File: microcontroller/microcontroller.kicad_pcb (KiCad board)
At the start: 2 copper layers, 70 x 39 mm, 46 parts, among them J1 Conn_01x05_Pin, J2 Conn_01x10_Pin, J3 USB_C_Receptacle, J4 Conn_01x04_Pin, SW1 SW_SPST, SW2 SW_SPST, SW3 SW_SPST, U1 DS3231MZ, U2 AMS1117-3.3, U3 STM32F103CBTx, Y1 8Mhz

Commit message: Changed connectors
Changed connector from mcu to power supply to idc.
All switches now use a straight pinheader, with no pullups (now using
mcu pulldowns).
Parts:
- removed the R1 at (137.3, 96.3)
- removed the R2 at (141.1, 96.3)
- removed the R3 at (144.8, 96.3)
- removed SW1, SW2, SW3: SW_SPST, Connector_PinHeader_2.54mm:PinHeader_1x02_P2.54mm_Vertical
- added J2: Conn_01x04_Pin, Connector_PinHeader_2.54mm:PinHeader_1x04_P2.54mm_Vertical, F.Cu at (142.1, 91.9)
- J1: value Conn_01x05_Pin -> Conn_01x04_Pin; footprint Connector_PinHeader_2.54mm:PinHeader_1x05_P2.54mm_Vertical -> Connector_PinHeader_2.54mm:PinHeader_1x04_P2.54mm_Vertical
- J3: renamed from J2; footprint Connector_PinHeader_2.54mm:PinHeader_1x10_P2.54mm_Vertical -> Connector_IDC:IDC-Header_2x05_P2.54mm_Vertical
- moved R3 23.3 mm to (119.9, 82.2), turned to 90 degrees
- moved D1 18.7 mm to (119.9, 85.3), turned to -90 degrees
- moved J3 17.0 mm to (178.4, 80.4), turned to 0 degrees
- moved JP1 9.43 mm to (119.9, 91.3), turned to 180 degrees
- moved R9 9.31 mm to (127.9, 99.9), turned to 180 degrees
- moved R8 5.26 mm to (130.9, 99.9), turned to 0 degrees
- moved J1 4.18 mm to (142.1, 99.9)
- moved U1 0.59 mm to (128.5, 92.1)
- moved C1 0.58 mm to (124.1, 90.6)
- renumbered J3 to J4, J4 to J5, R4 to R1, R5 to R2, R6 to R3, R7 to R4, R8 to R5, R9 to R6, R10 to R7, R11 to R8, R12 to R9
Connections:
- J1 pad 1: GND -> ADJUST_SW
- J1 pad 2: SECOND_SW_H -> MODE_SW
- J1 pad 3: MINUTE_SW_H -> POWER_SW
- J1 pad 4: HOUR_SW_H -> +3V3
- U3 pad 13: ADJUST_SW -> SECOND_SW_H
- U3 pad 14: MODE_SW -> MINUTE_SW_H
- U3 pad 15: POWER_SW -> HOUR_SW_H
- U3 pad 16: HOUR_SW_H -> POWER_SW
- U3 pad 17: MINUTE_SW_H -> MODE_SW
- U3 pad 18: SECOND_SW_H -> ADJUST_SW
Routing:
- net +3V3: track 162.1 -> 202.8 mm, vias 2 -> 0
- net VBUS: track 37.7 -> 59.8 mm
- net LATCH: track 11.3 -> 21.4 mm, vias 0 -> 2
- net OE: track 12.5 -> 17.5 mm, vias 0 -> 2
- net ADJUST_SW: track 20.3 -> 25.1 mm
- net CLK: track 12.0 -> 16.2 mm, vias 0 -> 2
- net MODE_SW: track 25.0 -> 27.7 mm
- net SECOND_SW_H: track 24.5 -> 22.2 mm
- net GND: track 41.8 -> 40.5 mm, vias 29 -> 26
- net SER: track 14.1 -> 12.9 mm
- net HOUR_SW_H: track 28.1 -> 28.9 mm
- net +BATT: track 45.8 -> 46.5 mm, vias 0 -> 2
- net MINUTE_SW_H: track 26.3 -> 25.6 mm
- net SDA: track 53.5 -> 52.9 mm

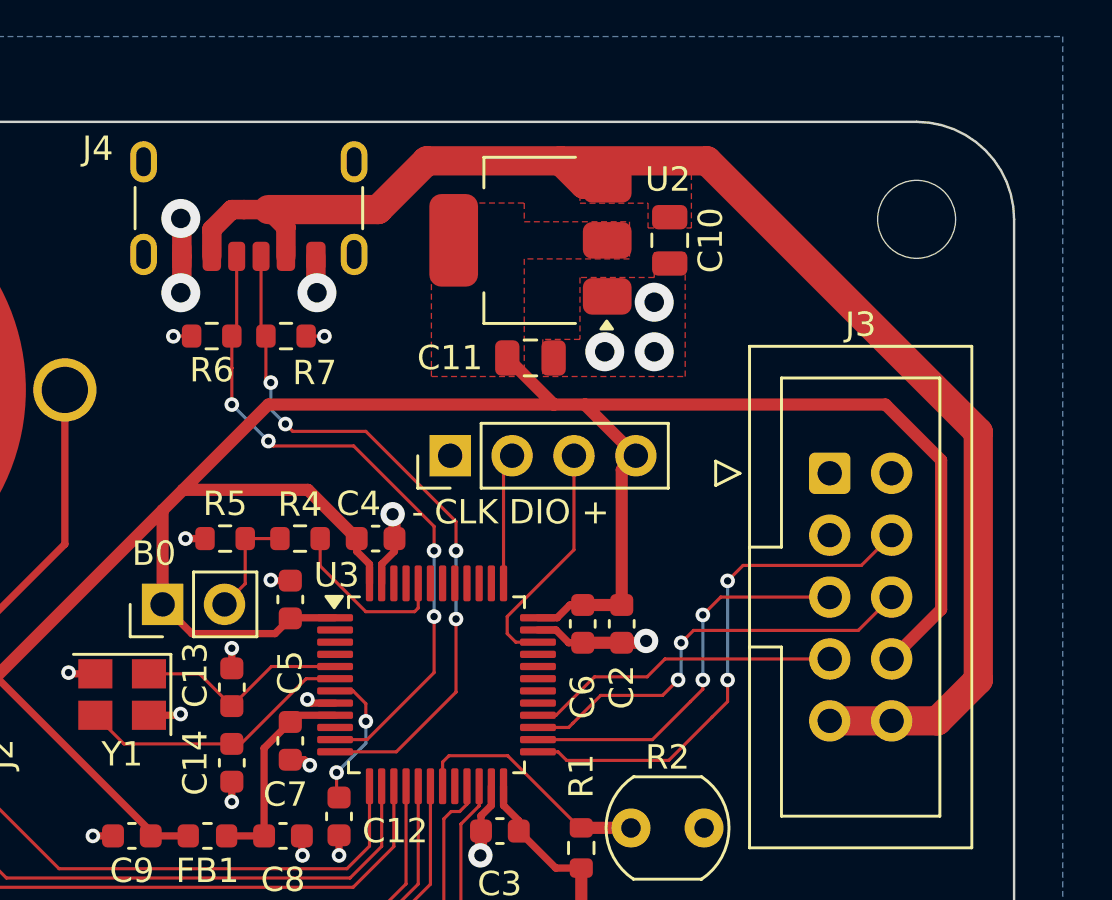
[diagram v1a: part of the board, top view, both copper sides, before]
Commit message: Added ESD protection
Added esd protection to the mcu board.
Also added breakout board for panel mounted switches.
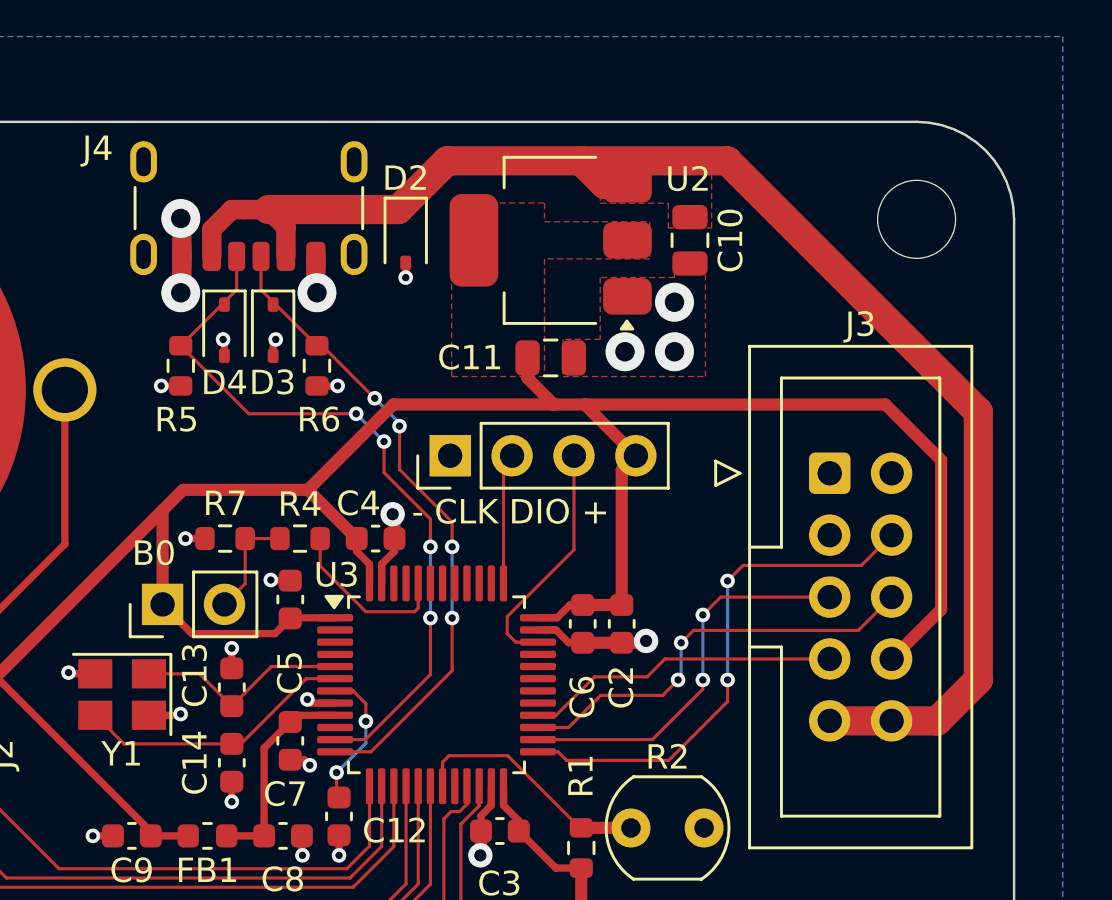
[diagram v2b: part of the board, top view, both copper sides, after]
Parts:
- added D2: D_Zener, Diode_SMD:D_SOD-323, F.Cu at (161.0, 70.7)
- added D3: D_Zener, Diode_SMD:D_SOD-323, F.Cu at (155.6, 74.5)
- added D4: D_Zener, Diode_SMD:D_SOD-323, F.Cu at (153.6, 74.5)
- moved R6 1.76 mm to (157.4, 76.0), turned to 90 degrees
- moved R5 1.76 mm to (151.8, 76.0), turned to 90 degrees
- moved C11 0.83 mm to (167.0, 75.7)
- moved U2 0.83 mm to (167.0, 70.9)
- moved C10 0.83 mm to (172.7, 70.9)
- renumbered R6 to R5, R7 to R6, R5 to R7
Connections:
- net ADJUST_SW renamed TOGGLE_SW_1
- net HOUR_SW_H renamed MECH_SW_3
- net MINUTE_SW_H renamed MECH_SW_2
- net MODE_SW renamed TOGGLE_SW_2
- net POWER_SW renamed TOGGLE_SW_3
- net SECOND_SW_H renamed MECH_SW_1
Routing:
- net +3V3: track 202.8 -> 197.3 mm
- net USB_CC1: track 28.9 -> 26.6 mm
- net USB_CC2: track 27.7 -> 30.0 mm
- net GND: track 40.5 -> 42.6 mm, vias 26 -> 29

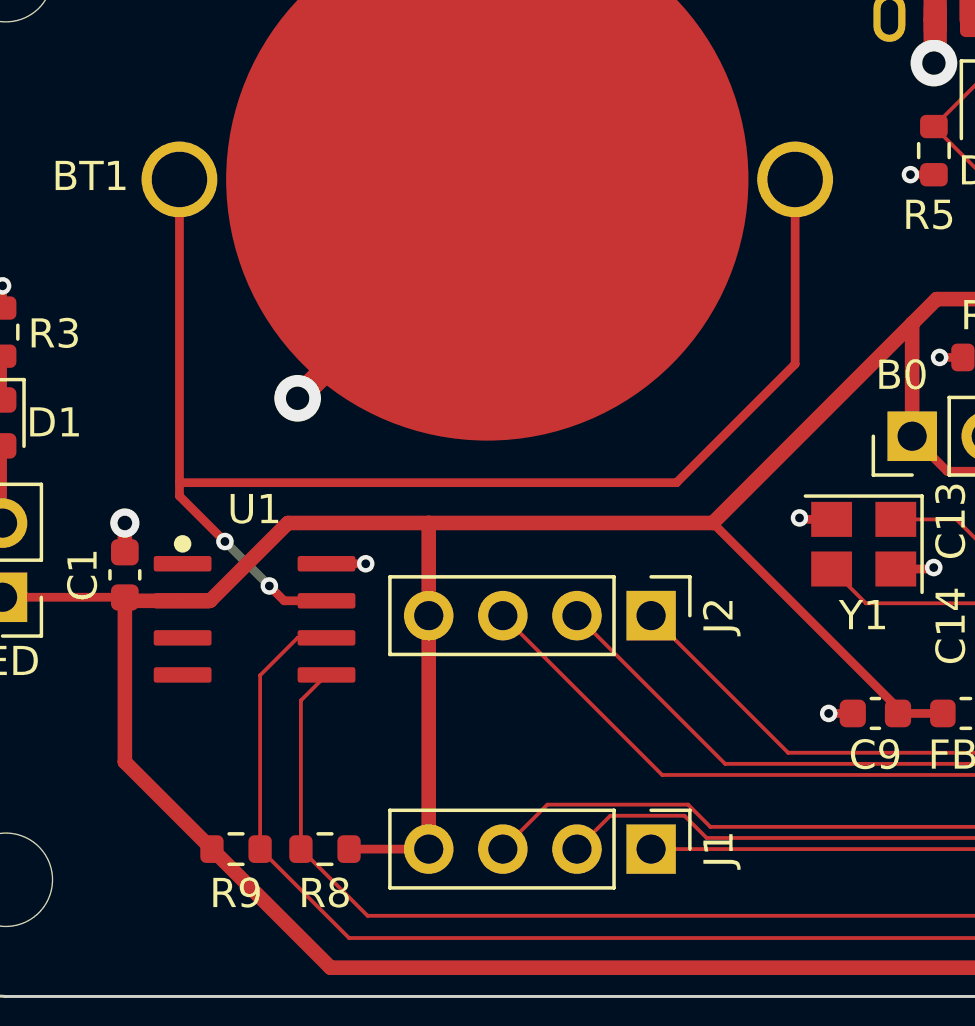
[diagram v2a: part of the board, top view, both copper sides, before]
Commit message: Added vents to case
Added vents to the underside of the case to encourage airflow.
Also fixed some stupid design mistakes on the PCBs. This is the night
before EMTH btw.
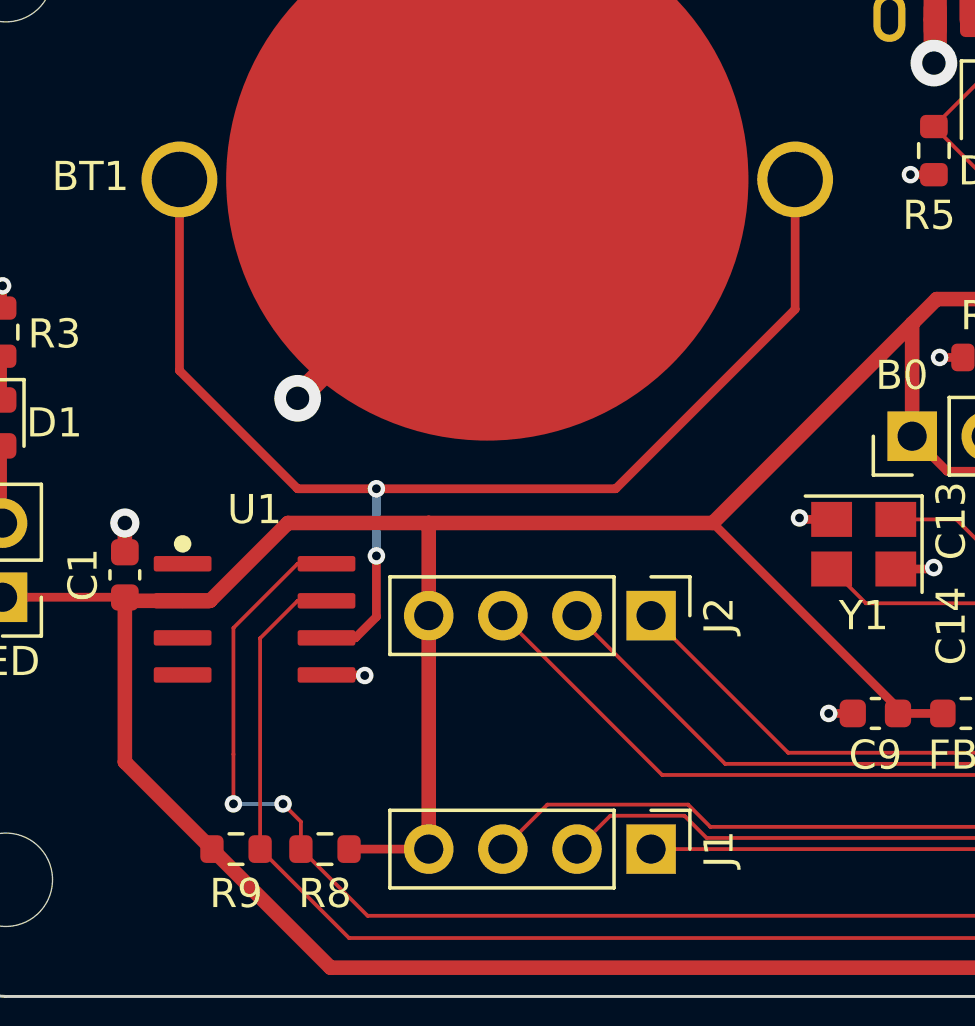
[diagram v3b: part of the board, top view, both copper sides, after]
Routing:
- net SCL: track 47.8 -> 55.1 mm, vias 0 -> 2
- net +BATT: track 46.5 -> 42.7 mm
- net SDA: track 52.9 -> 54.2 mm
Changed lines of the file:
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@@
 	(title_block
 		(title "Microcontroller PCB")
-		(date "2024-06-07")
-		(rev "0.1.2")
+		(date "2024-06-09")
+		(rev "0.1.3")
 	)
 	(layers
@@
 		)
 		(pad "5" smd roundrect
-			(at 2.465 -1.905)
+			(at 2.465 1.905)
 			(size 1.98 0.53)
 			(layers "F.Cu" "F.Paste" "F.Mask")
@@
 		)
 		(pad "6" smd roundrect
-			(at 2.465 -0.635)
+			(at 2.465 0.635)
 			(size 1.98 0.53)
 			(layers "F.Cu" "F.Paste" "F.Mask")
@@
 		)
 		(pad "7" smd roundrect
-			(at 2.465 0.635)
+			(at 2.465 -0.635)
 			(size 1.98 0.53)
 			(layers "F.Cu" "F.Paste" "F.Mask")
@@
 		)
 		(pad "8" smd roundrect
-			(at 2.465 1.905)
+			(at 2.465 -1.905)
 			(size 1.98 0.53)
 			(layers "F.Cu" "F.Paste" "F.Mask")
@@
 	)
 	(segment
+		(start 130.989 93.98)
+		(end 132.28 93.98)
+		(width 0.3)
+		(layer "F.Cu")
+		(net 1)
+	)
+	(segment
 		(start 157.394 76.837)
 		(end 158.24 76.837)
@@
 	)
 	(segment
+		(start 132.28 93.98)
+		(end 132.3 94)
+		(width 0.3)
+		(layer "F.Cu")
+		(net 1)
+	)
+	(segment
 		(start 151.85 71.52)
 		(end 151.85 72.968)
@@
 	)
 	(segment
-		(start 130.989 90.17)
-		(end 132.334 90.17)
-		(width 0.3)
-		(layer "F.Cu")
-		(net 1)
-	)
-	(segment
 		(start 153.9 93.075)
 		(end 153.9 93.9)
@@
 	)
 	(via
+		(at 132.3 94)
+		(size 0.6)
+		(drill 0.3)
+		(layers "F.Cu" "B.Cu")
+		(net 1)
+	)
+	(via
 		(at 153.543 74.93)
 		(size 0.6)
@@
 	)
 	(via
-		(at 132.334 90.17)
-		(size 0.6)
-		(drill 0.3)
-		(layers "F.Cu" "B.Cu")
-		(net 1)
-	)
-	(via
 		(at 151.806 73.012)
 		(size 1.6)
@@
 	)
 	(segment
-		(start 147.05 77)
-		(end 147.05 83.328)
+		(start 125.95 83.55)
+		(end 130 87.6)
 		(width 0.3)
 		(layer "F.Cu")
@@
 	)
 	(segment
-		(start 142.987 87.391)
-		(end 125.95 87.391)
+		(start 130 87.6)
+		(end 132.7 87.6)
 		(width 0.3)
 		(layer "F.Cu")
@@
 	)
 	(segment
-		(start 125.95 87.391)
-		(end 125.95 77)
+		(start 130.989 92.71)
+		(end 131.979 92.71)
 		(width 0.3)
 		(layer "F.Cu")
@@
 	)
 	(segment
-		(start 125.95 87.85)
-		(end 127.508 89.408)
+		(start 125.95 77)
+		(end 125.95 83.55)
 		(width 0.3)
 		(layer "F.Cu")
@@
 	)
 	(segment
-		(start 129.54 91.44)
-		(end 130.989 91.44)
+		(start 140.9 87.6)
+		(end 132.7 87.6)
 		(width 0.3)
 		(layer "F.Cu")
@@
 	)
 	(segment
-		(start 125.95 87.391)
-		(end 125.95 87.85)
+		(start 147.05 77)
+		(end 147.05 81.45)
 		(width 0.3)
 		(layer "F.Cu")
@@
 	)
 	(segment
-		(start 129.032 90.932)
-		(end 129.54 91.44)
+		(start 131.979 92.71)
+		(end 132.7 91.989)
 		(width 0.3)
 		(layer "F.Cu")
@@
 	)
 	(segment
-		(start 147.05 83.328)
-		(end 142.987 87.391)
+		(start 147.05 81.45)
+		(end 140.9 87.6)
+		(width 0.3)
+		(layer "F.Cu")
+		(net 2)
+	)
+	(segment
+		(start 132.7 91.989)
+		(end 132.7 89.9)
 		(width 0.3)
 		(layer "F.Cu")
@@
 	)
 	(via
-		(at 127.508 89.408)
+		(at 132.7 89.9)
 		(size 0.6)
 		(drill 0.3)
@@
 	)
 	(via
-		(at 129.032 90.932)
+		(at 132.7 87.6)
 		(size 0.6)
 		(drill 0.3)
@@
 	)
 	(segment
-		(start 127.508 89.408)
-		(end 129.032 90.932)
+		(start 132.7 89.9)
+		(end 132.7 87.6)
 		(width 0.3)
 		(layer "B.Cu")
@@
 	)
 	(segment
+		(start 129.667 88.773)
+		(end 127 91.44)
+		(width 0.5)
+		(layer "F.Cu")
+		(net 3)
+	)
+	(segment
+		(start 127 91.44)
+		(end 126.059 91.44)
+		(width 0.5)
+		(layer "F.Cu")
+		(net 3)
+	)
+	(segment
 		(start 152.1125 95.3)
 		(end 150.575 95.3)
@@
 	)
 	(segment
-		(start 129.667 88.773)
-		(end 127 91.44)
-		(width 0.5)
-		(layer "F.Cu")
-		(net 3)
-	)
-	(segment
 		(start 167.116 77.6)
 		(end 168.4 77.6)
@@
 	)
 	(segment
-		(start 127 91.44)
-		(end 126.059 91.44)
-		(width 0.5)
-		(layer "F.Cu")
-		(net 3)
-	)
-	(segment
 		(start 160.528 77.597)
 		(end 157.025 81.1)
@@
 	)
 	(segment
-		(start 130.112 94.857)
+		(start 127.8 92.369)
+		(end 127.8 96.7)
+		(width 0.13)
+		(layer "F.Cu")
+		(net 23)
+	)
+	(segment
+		(start 129.5 98.4)
+		(end 130.112 99.012)
+		(width 0.13)
+		(layer "F.Cu")
+		(net 23)
+	)
+	(segment
+		(start 130.112 99.012)
 		(end 130.112 99.949)
 		(width 0.13)
@@
 	)
 	(segment
-		(start 130.112 99.949)
-		(end 132.398 102.235)
+		(start 129.999 90.17)
+		(end 127.8 92.369)
 		(width 0.13)
 		(layer "F.Cu")
@@
 	)
 	(segment
-		(start 130.989 93.98)
-		(end 130.112 94.857)
+		(start 127.8 96.7)
+		(end 127.8 98.4)
+		(width 0.13)
+		(layer "F.Cu")
+		(net 23)
+	)
+	(segment
+		(start 130.989 90.17)
+		(end 129.999 90.17)
+		(width 0.13)
+		(layer "F.Cu")
+		(net 23)
+	)
+	(segment
+		(start 130.112 99.949)
+		(end 132.398 102.235)
 		(width 0.13)
 		(layer "F.Cu")
@@
 		(net 23)
 	)
+	(via
+		(at 127.8 98.4)
+		(size 0.6)
+		(drill 0.3)
+		(layers "F.Cu" "B.Cu")
+		(net 23)
+	)
+	(via
+		(at 129.5 98.4)
+		(size 0.6)
+		(drill 0.3)
+		(layers "F.Cu" "B.Cu")
+		(net 23)
+	)
 	(segment
-		(start 129.999 92.71)
-		(end 128.714 93.995)
+		(start 127.8 98.4)
+		(end 129.5 98.4)
 		(width 0.13)
-		(layer "F.Cu")
-		(net 24)
+		(layer "B.Cu")
+		(net 23)
 	)
 	(segment
-		(start 128.714 93.995)
-		(end 128.714 99.949)
+		(start 163.3 94.816338)
+		(end 164.05 94.066338)
 		(width 0.13)
 		(layer "F.Cu")
@@
 	)
 	(segment
-		(start 163.3 94.816338)
-		(end 164.05 94.066338)
+		(start 130.989 91.44)
+		(end 129.999 91.44)
 		(width 0.13)
 		(layer "F.Cu")
@@
 	)
 	(segment
+		(start 129.999 91.44)
+		(end 128.714 92.725)
+		(width 0.13)
+		(layer "F.Cu")
+		(net 24)
+	)
+	(segment
 		(start 131.762 102.997)
 		(end 160.303 102.997)
@@
 	)
 	(segment
-		(start 128.714 99.949)
-		(end 131.762 102.997)
+		(start 128.714 92.725)
+		(end 128.714 99.949)
 		(width 0.13)
 		(layer "F.Cu")
@@
 	)
 	(segment
-		(start 130.989 92.71)
-		(end 129.999 92.71)
+		(start 128.714 99.949)
+		(end 131.762 102.997)
 		(width 0.13)
 		(layer "F.Cu")

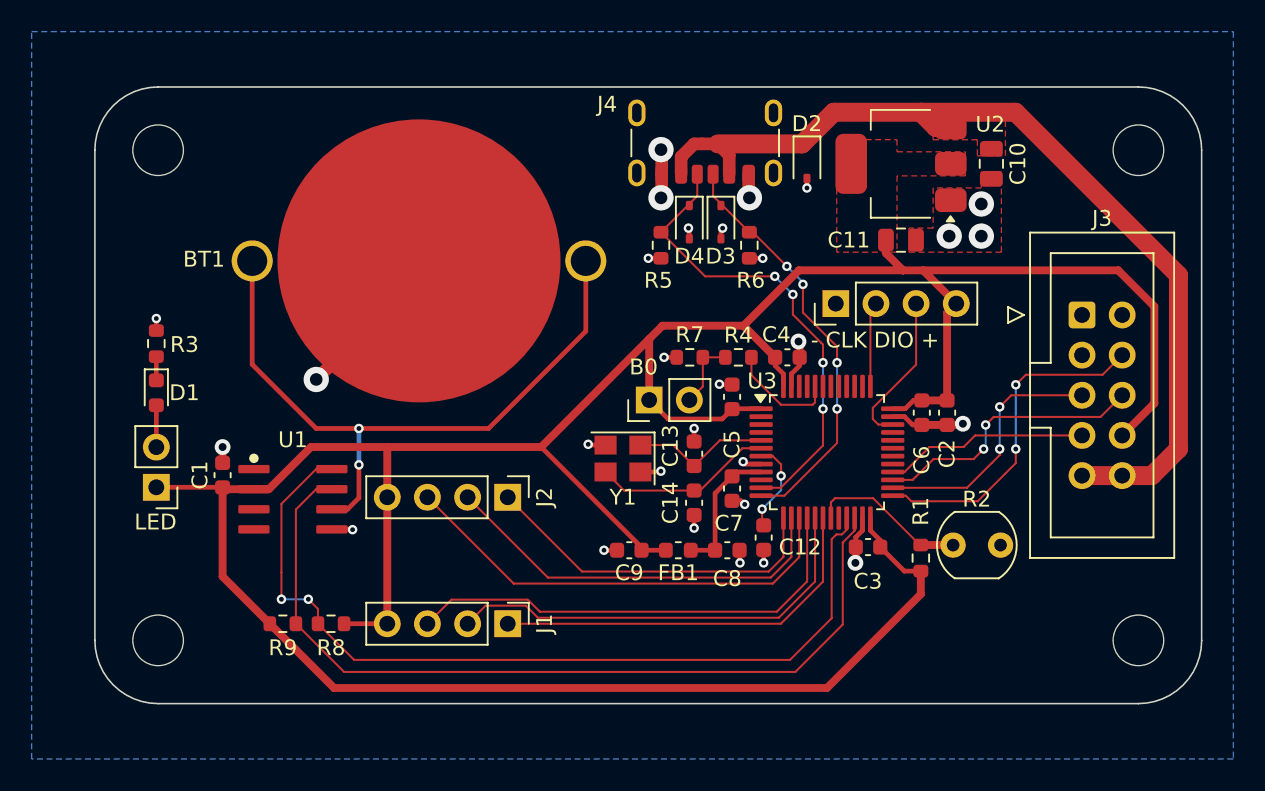
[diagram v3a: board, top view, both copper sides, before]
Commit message: Changed main PCB mount
Changed nixie board pcb mount, so now screws are visible on the front
side of the board instead of the back. Also changed mcu i2c pullups to
2k2.
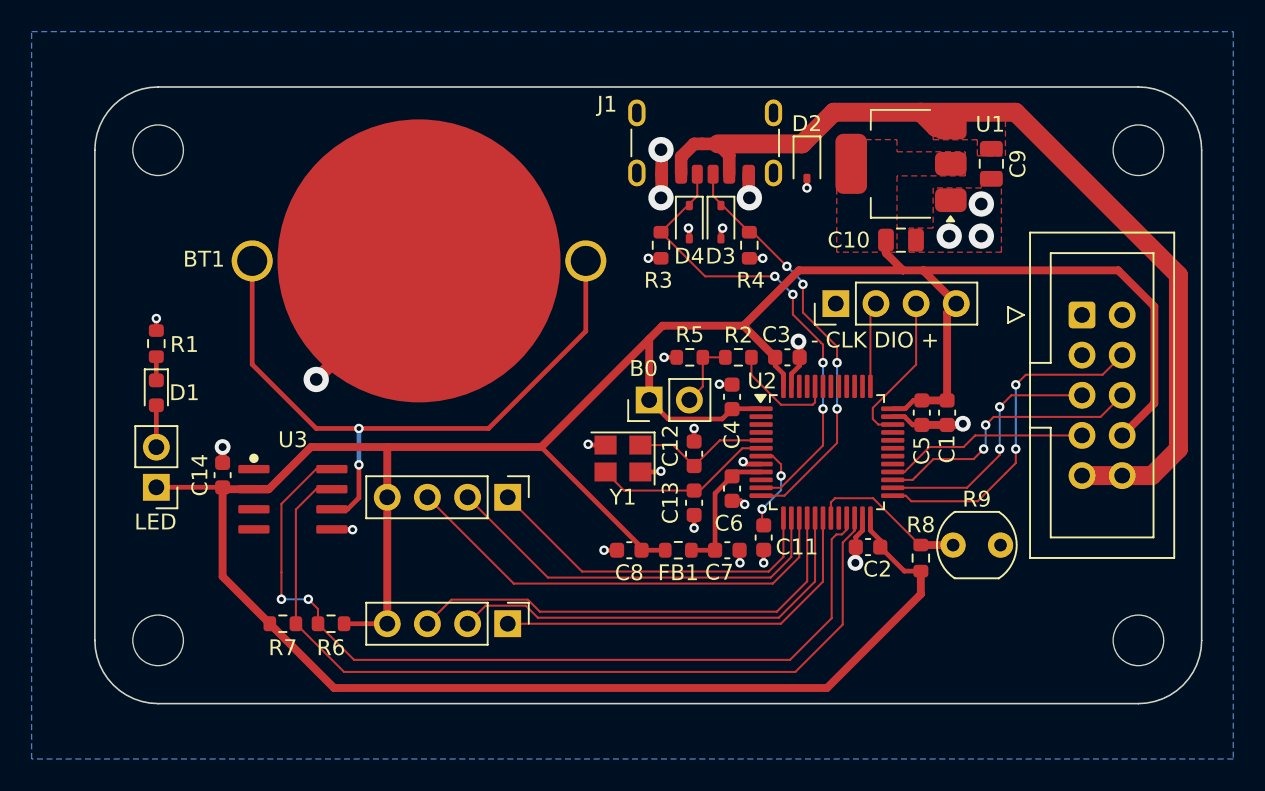
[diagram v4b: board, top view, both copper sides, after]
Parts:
- FB1: footprint Inductor_SMD:L_0603_1608Metric -> Resistor_SMD:R_0603_1608Metric
- R1: renamed from R3; value 1k5 -> 2k2
- R6: renamed from R8; value 1k5 -> 2k2
- R7: renamed from R9; value 1k5 -> 2k2
- renumbered C2 to C1, C11 to C10, C12 to C11, C13 to C12, C14 to C13, C1 to C14, C3 to C2, C4 to C3, C5 to C4, C6 to C5, C7 to C6, C8 to C7, C9 to C8, C10 to C9, J4 to J1, J5 to J2, J1 to J3, J2 to J4, J3 to J5, R4 to R2, R5 to R3, R6 to R4, R7 to R5, R1 to R8, R2 to R9, U2 to U1, U3 to U2, U1 to U3
